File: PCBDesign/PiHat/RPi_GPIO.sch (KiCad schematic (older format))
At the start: 1 part, among them J2 RPi_GPIO

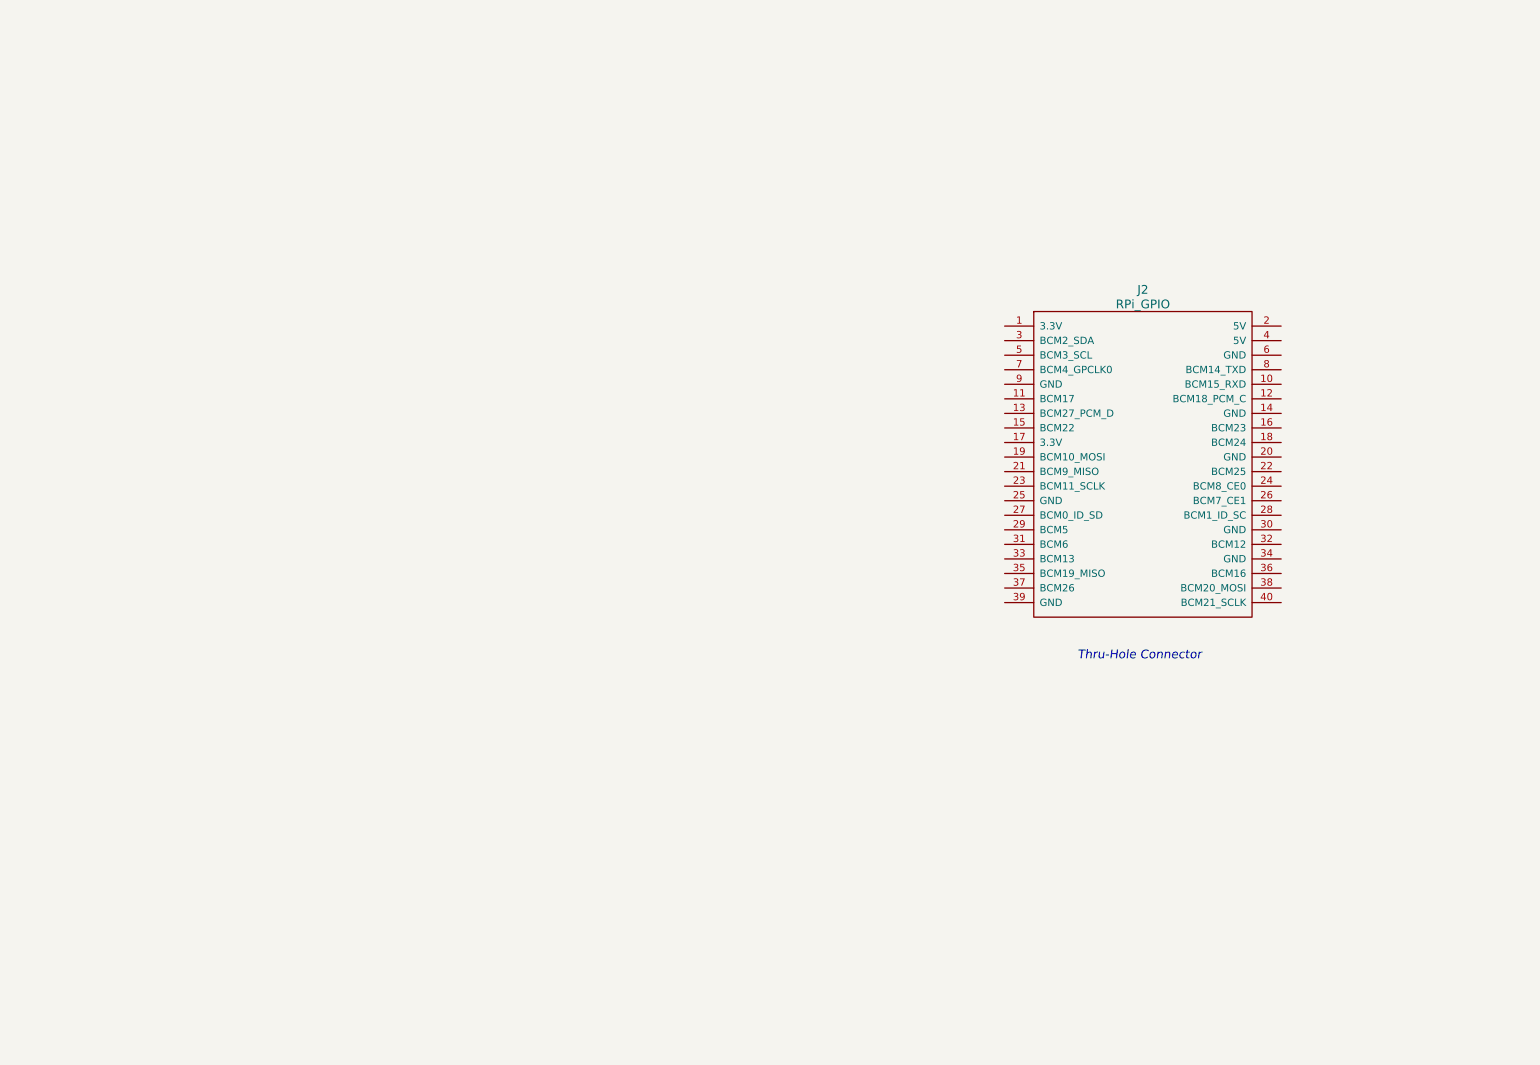
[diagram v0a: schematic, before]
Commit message: Work on schematic and loading in custom footprints
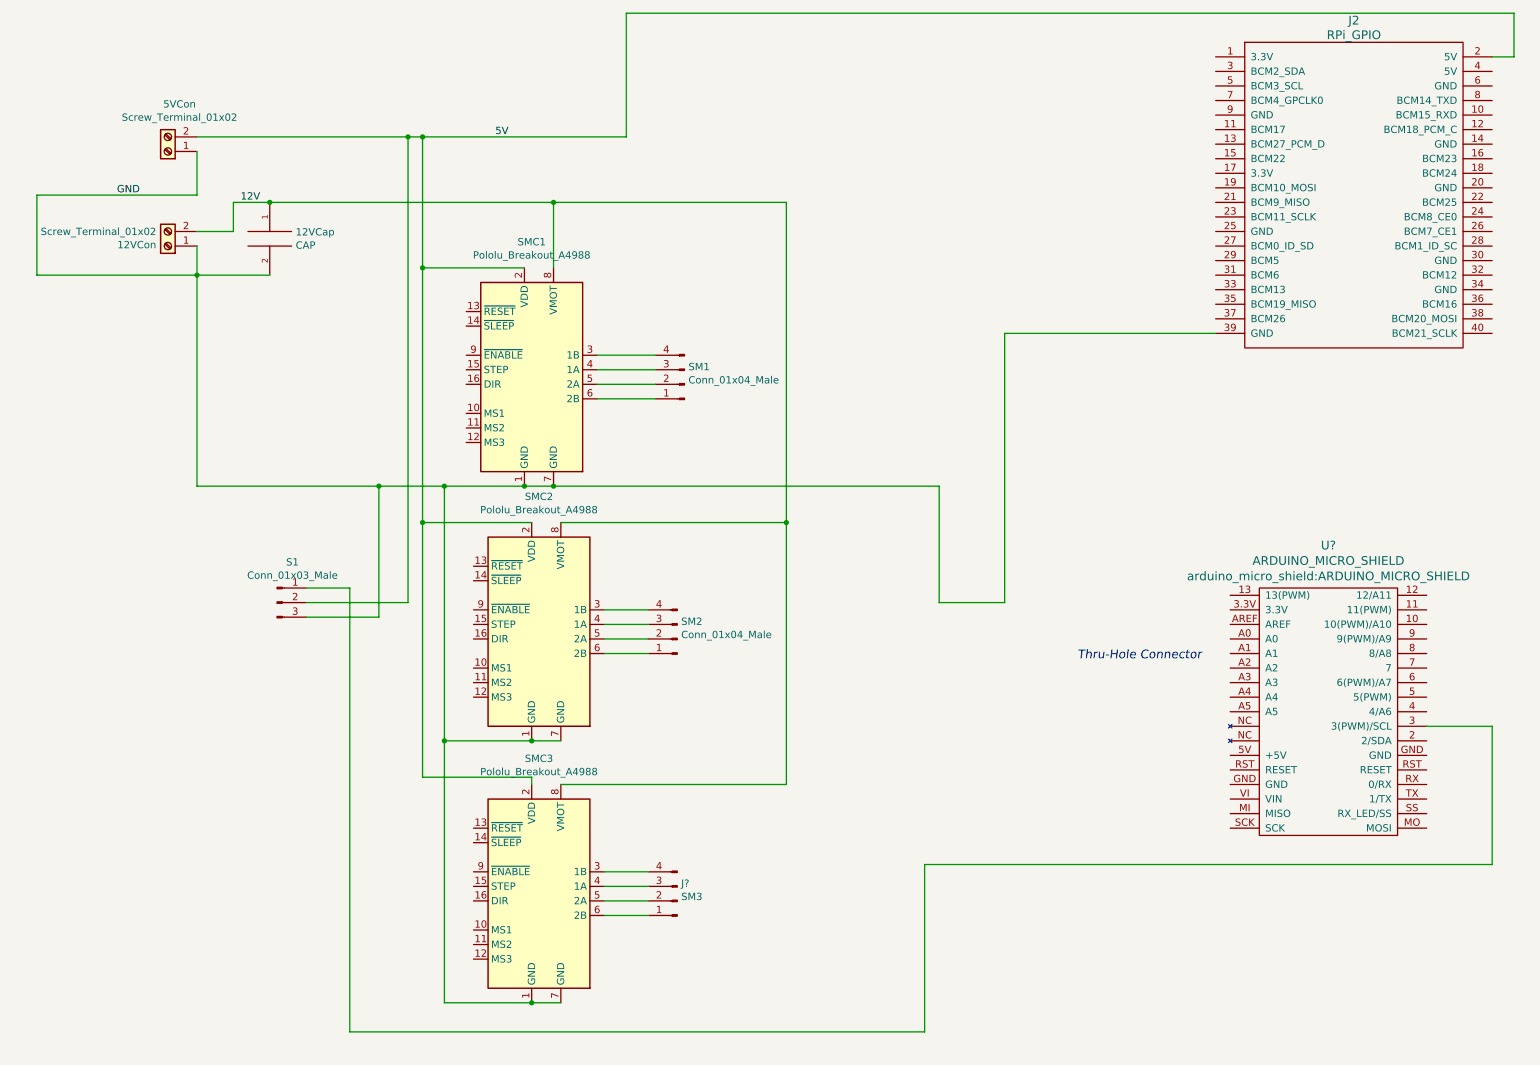
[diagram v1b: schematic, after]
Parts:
- added 12VCap: CAP, Capacitor_THT:CP_Axial_L10.0mm_D4.5mm_P15.00mm_Horizontal, symbol pspice:CAP
- added 12VCon, 5VCon: Screw_Terminal_01x02, symbol Connector:Screw_Terminal_01x02
- added J?: SM3, symbol Connector:Conn_01x04_Male
- added S1: Conn_01x03_Male, symbol Connector:Conn_01x03_Male
- added SM1, SM2: Conn_01x04_Male, symbol Connector:Conn_01x04_Male
- added SMC1, SMC2, SMC3: Pololu_Breakout_A4988, Module:Pololu_Breakout-16_15.2x20.3mm, symbol Driver_Motor:Pololu_Breakout_A4988
- added U?: ARDUINO_MICRO_SHIELD, arduino_micro_shield:ARDUINO_MICRO_SHIELD, symbol arduino_micro_shield:ARDUINO_MICRO_SHIELD
- J2: footprint RPi_Hat:Pin_Header_Straight_2x20 -> PiHat:Pin_Header_Straight_2x20
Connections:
- net 5V: now reaches J2.2 (5V)
- net 5V: now also 5VCon.2 (Pin_2), S1.2 (Pin_2), SMC1.2 (VDD), SMC2.2 (VDD), SMC3.2 (VDD)
- net GND: now reaches J2.39 (GND)
- net GND: now also 12VCap.2, 12VCon.1 (Pin_1), 5VCon.1 (Pin_1), S1.3 (Pin_3), SMC1.1 (GND), SMC1.7 (GND), SMC2.1 (GND), SMC2.7 (GND), SMC3.1 (GND), SMC3.7 (GND)
- new net: SM1.4 (Pin_4), SMC1.3 (1B)
- new net: SM1.3 (Pin_3), SMC1.4 (1A)
- new net: SM1.2 (Pin_2), SMC1.5 (2A)
- new net: SM1.1 (Pin_1), SMC1.6 (2B)
- new net: SM2.4 (Pin_4), SMC2.3 (1B)
- new net: SM2.3 (Pin_3), SMC2.4 (1A)
- new net: SM2.2 (Pin_2), SMC2.5 (2A)
- new net: SM2.1 (Pin_1), SMC2.6 (2B)
- new net: J?.4 (Pin_4), SMC3.3 (1B)
- new net: J?.3 (Pin_3), SMC3.4 (1A)
- new net: J?.2 (Pin_2), SMC3.5 (2A)
- new net: J?.1 (Pin_1), SMC3.6 (2B)
- new net: S1.1 (Pin_1), U?.3 (3(PWM)/SCL)
- new net 12V: 12VCap.1, 12VCon.2 (Pin_2), SMC1.8 (VMOT), SMC2.8 (VMOT), SMC3.8 (VMOT)
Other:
- moved on the sheet: J2

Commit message: First design, PiHat too small for our parts
Could possibly extend one side over the Pi
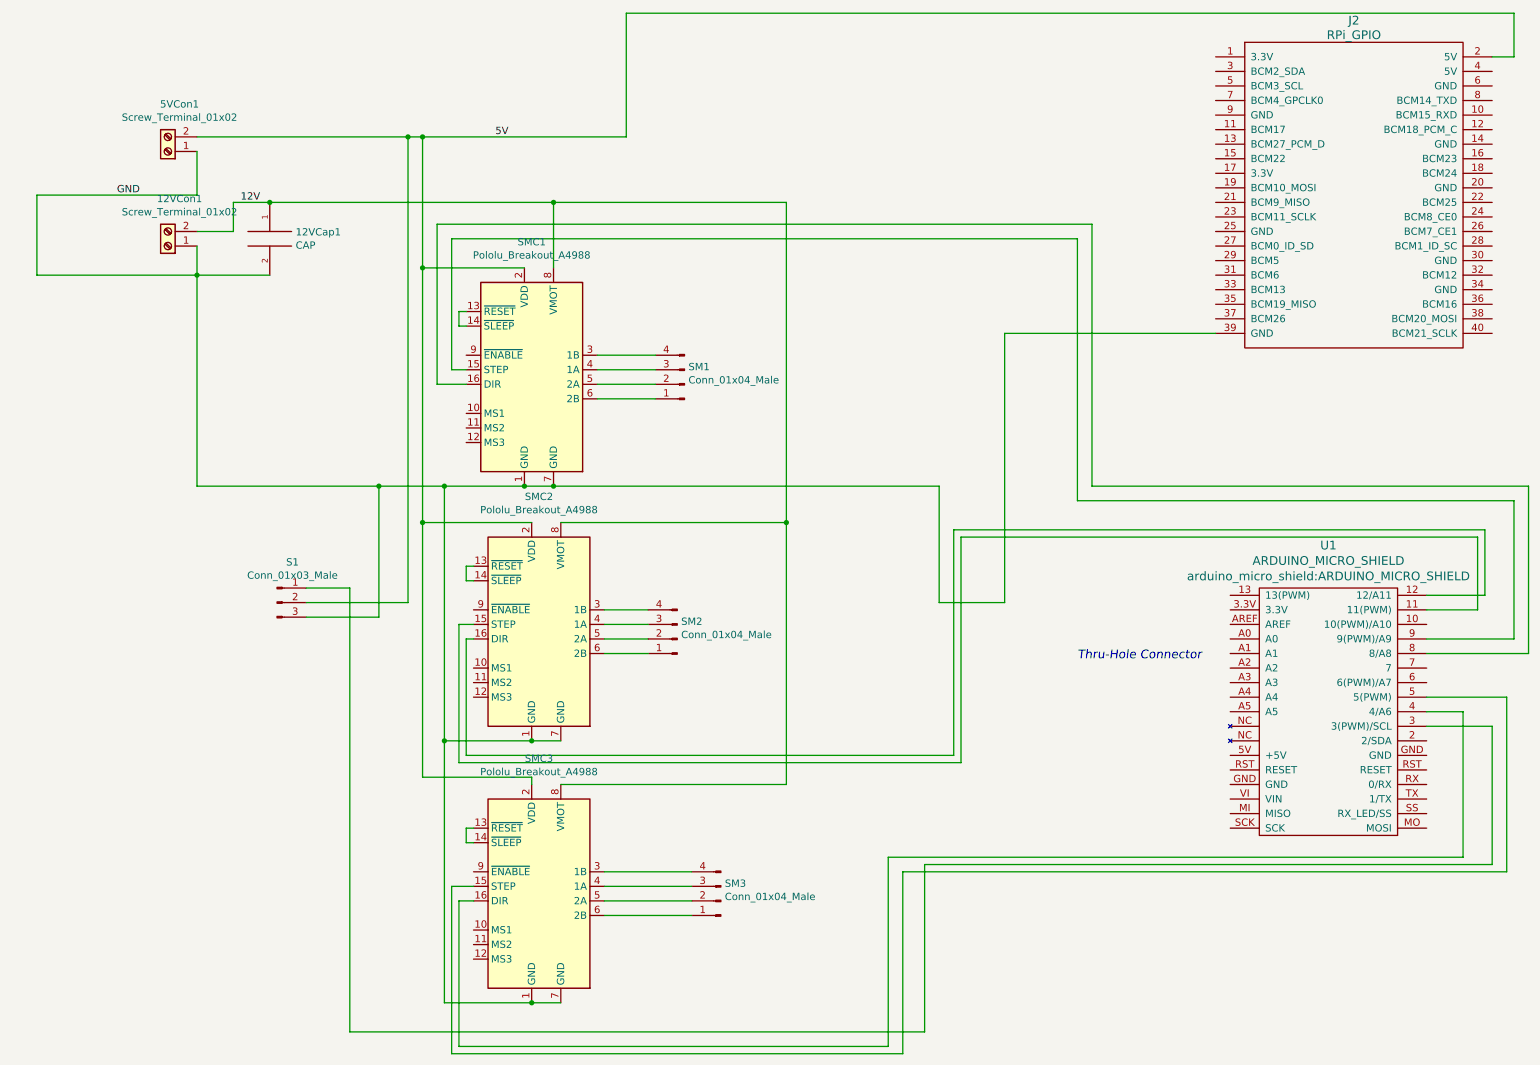
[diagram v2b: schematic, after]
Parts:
- removed J?: SM3, symbol Connector:Conn_01x04_Male
- added SM3: Conn_01x04_Male, Connector_PinHeader_2.54mm:PinHeader_1x04_P2.54mm_Vertical, symbol Connector:Conn_01x04_Male
- 12VCon1: renamed from 12VCon; footprint (none) -> TerminalBlock:TerminalBlock_bornier-2_P5.08mm
- 5VCon1: renamed from 5VCon; footprint (none) -> TerminalBlock:TerminalBlock_bornier-2_P5.08mm
- S1: footprint (none) -> Connector_PinHeader_2.54mm:PinHeader_1x03_P2.54mm_Vertical
- SM1, SM2: footprint (none) -> Connector_PinHeader_2.54mm:PinHeader_1x04_P2.54mm_Vertical
- gave numbers to parts that had none: 1
- renumbered 12VCap to 12VCap1
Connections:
- net at SMC1.13 (~RESET): now also SMC1.14 (~SLEEP)
- net at SMC1.15 (STEP): now also U1.9 (9(PWM)/A9)
- net at SMC1.16 (DIR): now also U1.8 (8/A8)
- net at SMC2.13 (~RESET): now also SMC2.14 (~SLEEP)
- net at SMC2.15 (STEP): now also U1.11 (11(PWM))
- net at SMC2.16 (DIR): now also U1.12 (12/A11)
- net at SMC3.13 (~RESET): now also SMC3.14 (~SLEEP)
- net at SMC3.15 (STEP): now also U1.5 (5(PWM))
- net at SMC3.16 (DIR): now also U1.4 (4/A6)
- net at SMC3.3 (1B): now also SM3.4 (Pin_4)
- net at SMC3.4 (1A): now also SM3.3 (Pin_3)
- net at SMC3.5 (2A): now also SM3.2 (Pin_2)
- net at SMC3.6 (2B): now also SM3.1 (Pin_1)
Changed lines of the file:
@@
 EESchema Schematic File Version 4
+LIBS:RPi_Hat-cache
 EELAYER 26 0
 EELAYER END
 $Descr A4 11693 8268
 encoding utf-8
-Sheet 1 1
+Sheet 1 2
 Title ""
 Date ""
@@
 $EndComp
 $Comp
-L arduino_micro_shield:ARDUINO_MICRO_SHIELD U?
+L arduino_micro_shield:ARDUINO_MICRO_SHIELD U1
 U 1 1 5C782D02
 P 10000 6200
-F 0 "U?" V 11993 6675 60  0000 C CNN
+F 0 "U1" V 11993 6675 60  0000 C CNN
 F 1 "ARDUINO_MICRO_SHIELD" V 11887 6675 60  0000 C CNN
 F 2 "arduino_micro_shield:ARDUINO_MICRO_SHIELD" V 11781 6675 60  0000 C CNN
@@
 $EndComp
 $Comp
-L pspice:CAP 12VCap
+L pspice:CAP 12VCap1
 U 1 1 5C782DDC
 P 2250 2100
-F 0 "12VCap" H 2428 2146 50  0000 L CNN
+F 0 "12VCap1" H 2428 2146 50  0000 L CNN
 F 1 "CAP" H 2428 2055 50  0000 L CNN
 F 2 "Capacitor_THT:CP_Axial_L10.0mm_D4.5mm_P15.00mm_Horizontal" H 2250 2100 50  0001 C CNN
@@
 $EndComp
 $Comp
-L Connector:Screw_Terminal_01x02 5VCon
+L Connector:Screw_Terminal_01x02 5VCon1
 U 1 1 5C782FA6
 P 1550 1500
-F 0 "5VCon" H 1470 1175 50  0000 C CNN
+F 0 "5VCon1" H 1470 1175 50  0000 C CNN
 F 1 "Screw_Terminal_01x02" H 1470 1266 50  0000 C CNN
-F 2 "" H 1550 1500 50  0001 C CNN
+F 2 "TerminalBlock:TerminalBlock_bornier-2_P5.08mm" H 1550 1500 50  0001 C CNN
 F 3 "~" H 1550 1500 50  0001 C CNN
 	1    1550 1500
@@
 $EndComp
 $Comp
-L Connector:Screw_Terminal_01x02 12VCon
+L Connector:Screw_Terminal_01x02 12VCon1
 U 1 1 5C7830BE
 P 1550 2150
-F 0 "12VCon" H 1630 2142 50  0000 L CNN
-F 1 "Screw_Terminal_01x02" H 1630 2051 50  0000 L CNN
-F 2 "" H 1550 2150 50  0001 C CNN
+F 0 "12VCon1" H 1470 1825 50  0000 C CNN
+F 1 "Screw_Terminal_01x02" H 1470 1916 50  0000 C CNN
+F 2 "TerminalBlock:TerminalBlock_bornier-2_P5.08mm" H 1550 2150 50  0001 C CNN
 F 3 "~" H 1550 2150 50  0001 C CNN
 	1    1550 2150
@@
 F 0 "SM1" H 5073 2980 50  0000 R CNN
 F 1 "Conn_01x04_Male" H 5073 3071 50  0000 R CNN
-F 2 "" H 5100 3100 50  0001 C CNN
+F 2 "Connector_PinHeader_2.54mm:PinHeader_1x04_P2.54mm_Vertical" H 5100 3100 50  0001 C CNN
 F 3 "~" H 5100 3100 50  0001 C CNN
 	1    5100 3100
-	-1   0    0    1
-$EndComp
-$Comp
-L Connector:Conn_01x04_Male J?
-U 1 1 5C783540
-P 5050 6650
-F 0 "J?" H 5023 6530 50  0000 R CNN
-F 1 "SM3" H 5023 6621 50  0000 R CNN
-F 2 "" H 5050 6650 50  0001 C CNN
-F 3 "~" H 5050 6650 50  0001 C CNN
-	1    5050 6650
 	-1   0    0    1
 $EndComp
@@
 F 0 "SM2" H 5023 4730 50  0000 R CNN
 F 1 "Conn_01x04_Male" H 5023 4821 50  0000 R CNN
-F 2 "" H 5050 4850 50  0001 C CNN
+F 2 "Connector_PinHeader_2.54mm:PinHeader_1x04_P2.54mm_Vertical" H 5050 4850 50  0001 C CNN
 F 3 "~" H 5050 4850 50  0001 C CNN
 	1    5050 4850
 	-1   0    0    1
 $EndComp
-Wire Wire Line
-	4550 6450 4850 6450
-Wire Wire Line
-	4550 6550 4850 6550
-Wire Wire Line
-	4550 6650 4850 6650
-Wire Wire Line
-	4550 6750 4850 6750
 Wire Wire Line
 	1750 1500 1750 1800
@@
 F 0 "S1" H 2406 4878 50  0000 C CNN
 F 1 "Conn_01x03_Male" H 2406 4787 50  0000 C CNN
-F 2 "" H 2300 4600 50  0001 C CNN
+F 2 "Connector_PinHeader_2.54mm:PinHeader_1x03_P2.54mm_Vertical" H 2300 4600 50  0001 C CNN
 F 3 "~" H 2300 4600 50  0001 C CNN
 	1    2300 4600
@@
 	5800 5850 4250 5850
 Connection ~ 5800 4050
+Wire Wire Line
+	3650 6150 3600 6150
+Wire Wire Line
+	3600 6150 3600 6250
+Wire Wire Line
+	3600 6250 3650 6250
+Wire Wire Line
+	3650 4350 3600 4350
+Wire Wire Line
+	3600 4350 3600 4450
+Wire Wire Line
+	3600 4450 3650 4450
+Wire Wire Line
+	3600 2600 3550 2600
+Wire Wire Line
+	3550 2600 3550 2700
+Wire Wire Line
+	3550 2700 3600 2700
+Wire Wire Line
+	3600 3100 3400 3100
+Wire Wire Line
+	3400 3100 3400 2000
+Wire Wire Line
+	3400 2000 7900 2000
+Wire Wire Line
+	7900 2000 7900 3800
+Wire Wire Line
+	7900 3800 10900 3800
+Wire Wire Line
+	10900 3800 10900 4950
+Wire Wire Line
+	10900 4950 10200 4950
+Wire Wire Line
+	3600 3000 3500 3000
+Wire Wire Line
+	3500 3000 3500 2100
+Wire Wire Line
+	3500 2100 7800 2100
+Wire Wire Line
+	7800 2100 7800 3900
+Wire Wire Line
+	7800 3900 10800 3900
+Wire Wire Line
+	10800 3900 10800 4850
+Wire Wire Line
+	10800 4850 10200 4850
+Wire Wire Line
+	10200 4550 10600 4550
+Wire Wire Line
+	10600 4550 10600 4100
+Wire Wire Line
+	10600 4100 6950 4100
+Wire Wire Line
+	6950 4100 6950 5650
+Wire Wire Line
+	6950 5650 3600 5650
+Wire Wire Line
+	3600 5650 3600 4850
+Wire Wire Line
+	3600 4850 3650 4850
+Wire Wire Line
+	3650 4750 3550 4750
+Wire Wire Line
+	3550 4750 3550 5700
+Wire Wire Line
+	3550 5700 7000 5700
+Wire Wire Line
+	7000 5700 7000 4150
+Wire Wire Line
+	7000 4150 10550 4150
+Wire Wire Line
+	10550 4150 10550 4650
+Wire Wire Line
+	10550 4650 10200 4650
+Wire Wire Line
+	3650 6650 3550 6650
+Wire Wire Line
+	3550 6650 3550 7650
+Wire Wire Line
+	3550 7650 6500 7650
+Wire Wire Line
+	6500 7650 6500 6350
+Wire Wire Line
+	6500 6350 10450 6350
+Wire Wire Line
+	10450 6350 10450 5350
+Wire Wire Line
+	10450 5350 10200 5350
+Wire Wire Line
+	3650 6550 3500 6550
+Wire Wire Line
+	3500 6550 3500 7700
+Wire Wire Line
+	3500 7700 6600 7700
+Wire Wire Line
+	6600 7700 6600 6450
+Wire Wire Line
+	6600 6450 10750 6450
+Wire Wire Line
+	10750 6450 10750 5250
+Wire Wire Line
+	10750 5250 10200 5250
+$Comp
+L Connector:Conn_01x04_Male SM3
+U 1 1 5C7AD885
+P 5350 6650
+F 0 "SM3" H 5323 6530 50  0000 R CNN
+F 1 "Conn_01x04_Male" H 5323 6621 50  0000 R CNN
+F 2 "Connector_PinHeader_2.54mm:PinHeader_1x04_P2.54mm_Vertical" H 5350 6650 50  0001 C CNN
+F 3 "~" H 5350 6650 50  0001 C CNN
+	1    5350 6650
+	-1   0    0    1
+$EndComp
+Wire Wire Line
+	4550 6450 5150 6450
+Wire Wire Line
+	4550 6550 5150 6550
+Wire Wire Line
+	4550 6650 5150 6650
+Wire Wire Line
+	4550 6750 5150 6750
 $EndSCHEMATC
